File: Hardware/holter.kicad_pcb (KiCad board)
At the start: 6 copper layers, 33.5 x 48 mm, 261 parts, among them CN1 2TAP, CN2 2TAP, CN3 3TAP, IC1 256kx8, M1 USB_Power_Module, M2 USB_Power_Module, P1 CONN_01X07, P2 PROG, P3 SCREW, P4 BAT-, Q1 PMF170XP, Q2 PMF170XP, Q3 NTR4101PT1G, Q4 PMF170XP, Q5 PMF170XP, U1 TXB0106, U10 TS5A3159, U11 TS5A3159, U12 ESD_PROTECTOR, U13 ESD_PROTECTOR, U14 ESD_PROTECTOR, U15 ESD_PROTECTOR, U16 ESD_PROTECTOR, U17 ESD_PROTECTOR, U18 ESD_PROTECTOR, U19 ESD_PROTECTOR, U2 TXB0106, U20 ESD_PROTECTOR, U21 ESD_PROTECTOR, U22 ESD_PROTECTOR, U23 ESD_PROTECTOR, U24 TLV61220, U25 TLV61220, U26 TLV61220, U27 LM3671, U28 DS2710, U29 LIS2DH12, U3 TiWi-uB2, U4 STM32F4x1_64, U5 uSD, U6 ADS1298, U7 USBULC6-2M6, U8 USB2641, U9 OPA379, X1 32768, Y1 24 MHz, Y2 10 MHz

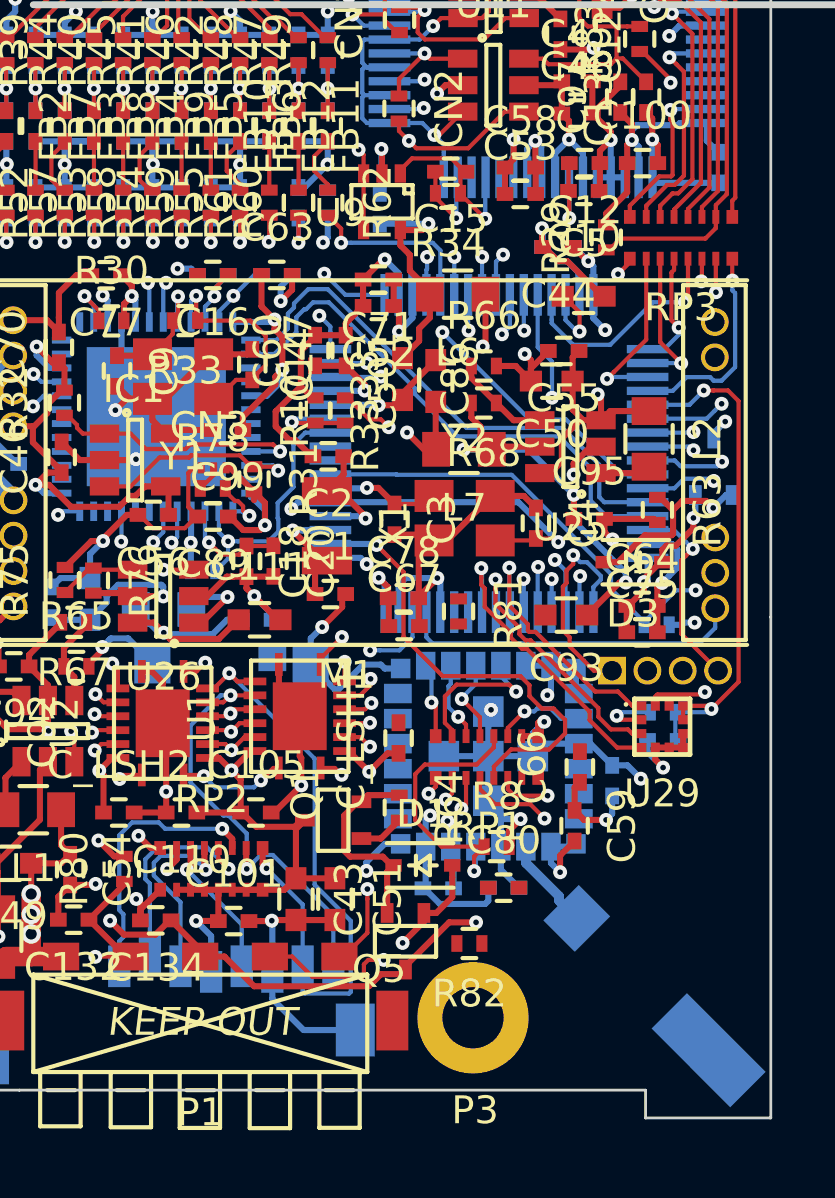
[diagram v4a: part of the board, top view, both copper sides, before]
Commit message: More PCB traces.
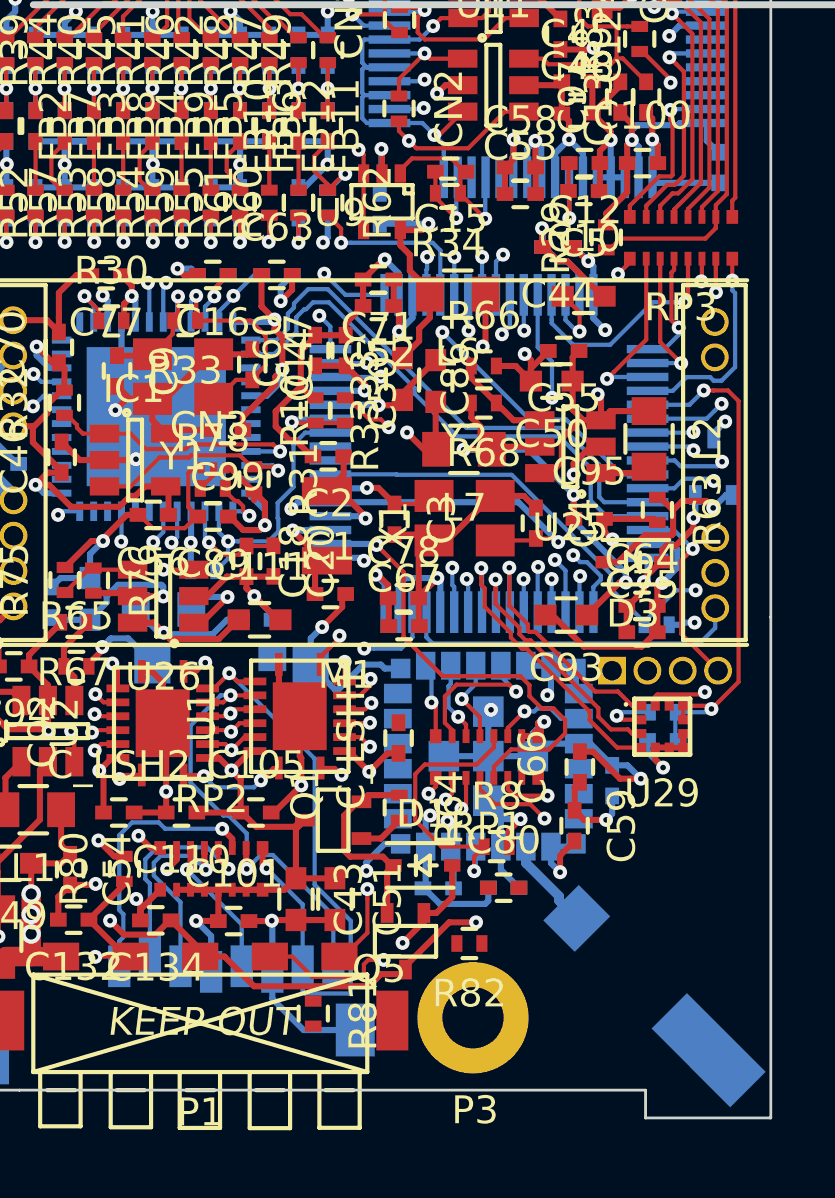
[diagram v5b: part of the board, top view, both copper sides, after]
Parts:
- moved R81 15.4 mm to (88.6, 79.2)
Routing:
- net GND: track 263.4 -> 271.5 mm
- net Net-(FB13-Pad1): track 2.16 -> 3.90 mm, vias 0 -> 1
- net G_PWM: track 0.00 -> 1.63 mm, vias 0 -> 1
- net R_PWM: track 0.00 -> 1.21 mm, vias 0 -> 1
- net SDIO_D1: track 18.8 -> 19.6 mm
- net SDIO_D2: track 13.4 -> 14.1 mm
- net SWCLK: track 8.13 -> 7.56 mm
- net SDIO_D0: track 18.7 -> 19.3 mm
- net RX: track 32.7 -> 32.2 mm

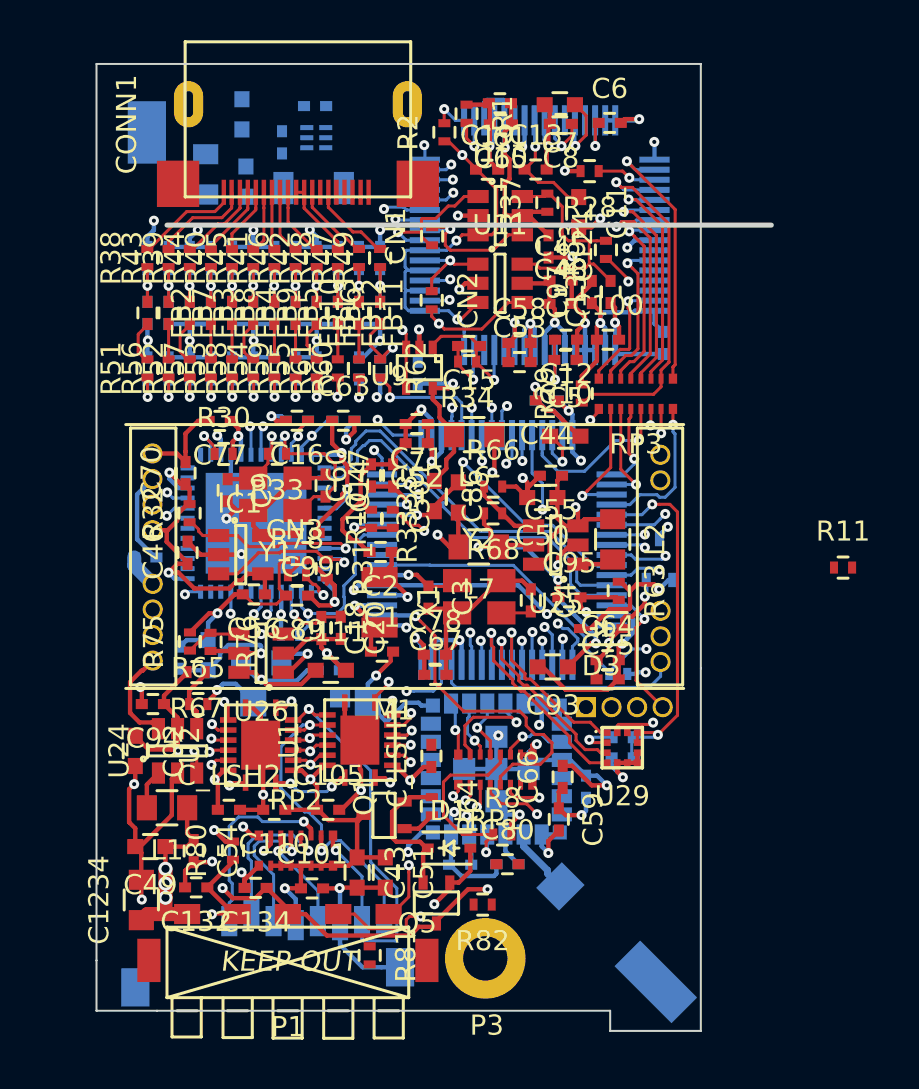
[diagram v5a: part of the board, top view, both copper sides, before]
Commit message: Everything is connected on the main board.
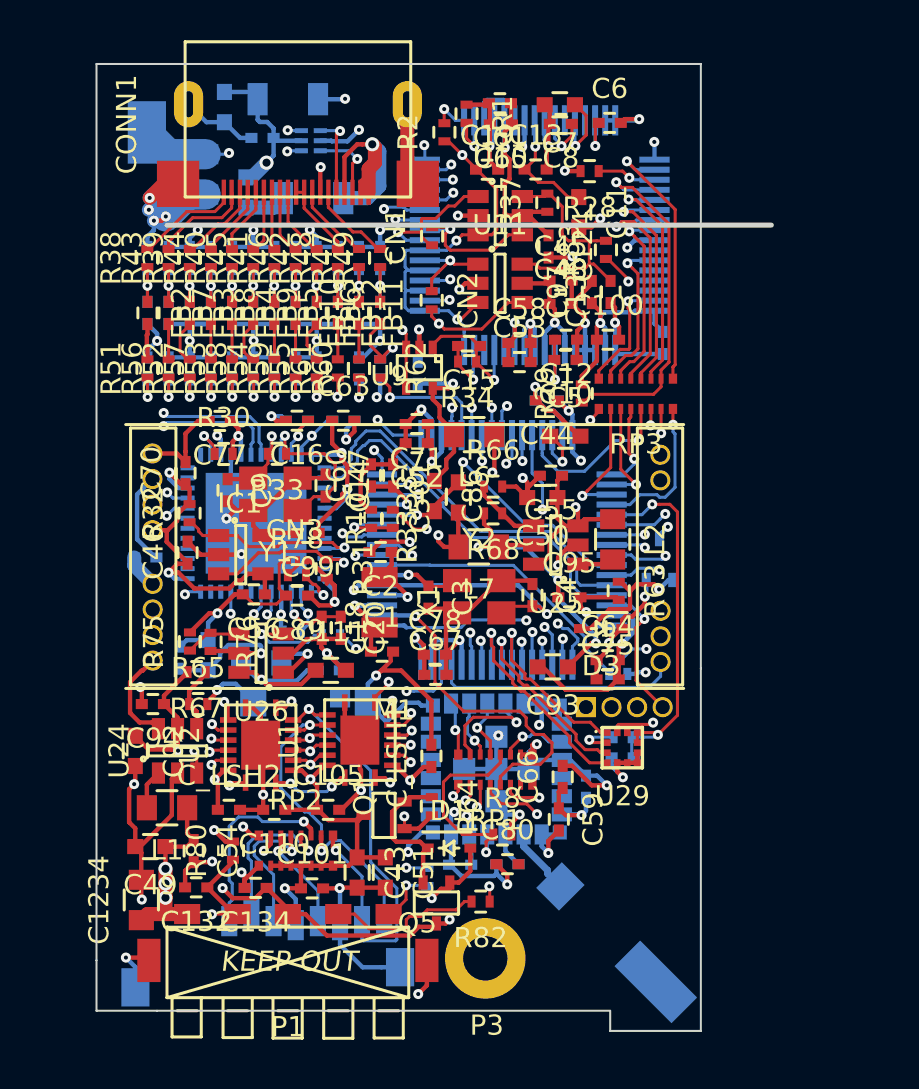
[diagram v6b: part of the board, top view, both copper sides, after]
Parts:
- C125: value 100nF -> 47uF; footprint Capacitors_SMD:C_0402 -> Capacitors_SMD:C_1206
- R11, R81: moved to B.Cu
- moved R11 25.6 mm to (86.6, 63.4), turned to 180 degrees
- moved R81 4.83 mm to (91.4, 75.4)
- moved C125 1.39 mm to (84.5, 36.8)
- moved C137 0.99 mm to (83.2, 38.7), turned to 180 degrees
- moved C115 0.94 mm to (81.3, 37.1)
- moved FB1 0.54 mm to (82.4, 41.4)
- moved F1 0.50 mm to (85.8, 41.7)
- moved U7 0.31 mm to (85.6, 38.8)
- moved C4 0.27 mm to (96.6, 61.4)
- moved R36 0.18 mm to (84.7, 63.2)
- moved R82 0.18 mm to (94.1, 76.6)
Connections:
- net DM renamed D-
- net DP renamed D+
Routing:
- net GND: track 271.5 -> 308.9 mm, vias 58 -> 67
- net R_PWM: track 1.21 -> 23.4 mm, vias 1 -> 2
- net +3V3: track 110.3 -> 131.1 mm
- net +5V: track 50.4 -> 68.2 mm, vias 2 -> 3
- net ~SD_EN: track 1.63 -> 18.7 mm, vias 0 -> 2
- net G_PWM: track 1.63 -> 18.3 mm, vias 1 -> 2
- net BAT+: track 60.2 -> 74.5 mm
- net VBAT: track 1.25 -> 14.6 mm
- net Net-(CONN1-Pad16): track 0.00 -> 12.8 mm, vias 0 -> 1
- net Net-(R11-Pad1): track 0.00 -> 10.2 mm, vias 0 -> 2
- net +2.8VD: track 44.5 -> 54.7 mm
- net D+: track 18.5 -> 28.5 mm, vias 1 -> 2
- net D-: track 18.4 -> 28.1 mm, vias 1 -> 2
- net Net-(M1-Pad3): track 24.5 -> 33.1 mm, vias 0 -> 1
- net VCPU: track 45.1 -> 53.2 mm
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
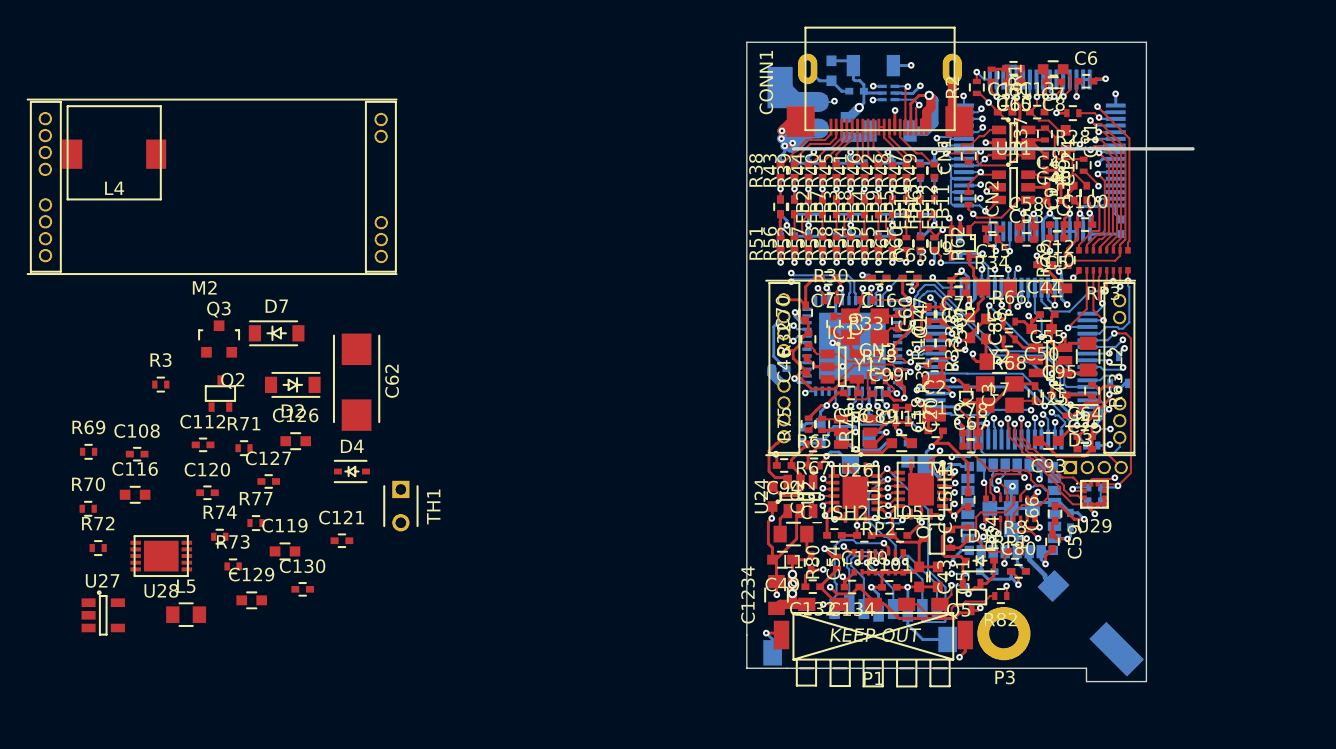
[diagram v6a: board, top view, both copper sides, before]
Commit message: New footprint for the inductor of the charger.
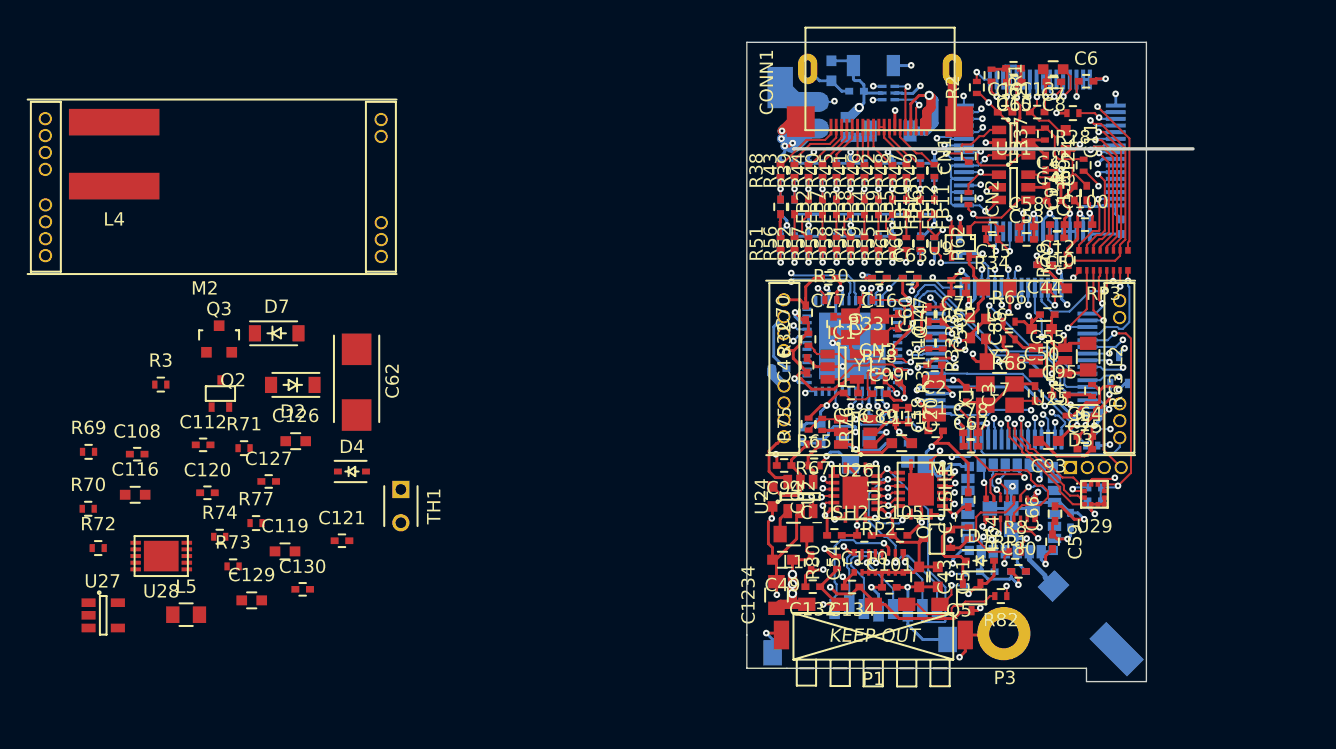
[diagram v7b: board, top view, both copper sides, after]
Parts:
- L4: value 15uH SLF7055T-150M2R1-3PF -> 15uH SRR6038; footprint Footprints:SLF7055 -> Footprints:SRR6038
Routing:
- net GND: track 308.9 -> 311.9 mm
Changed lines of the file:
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@@
   (general
     (links 682)
-    (no_connects 68)
-    (area 15.2726 20.8 109.150001 85.650001)
+    (no_connects 66)
+    (area 74.949999 34.949999 105.050001 83.050001)
     (thickness 1.6)
     (drawings 77)
-    (tracks 2962)
+    (tracks 2964)
     (zones 0)
     (modules 261)
@@
     )
   )
-  (module Footprints:SLF7055 (layer Front)
-    (at 27.5 43.4)
-    (fp_text reference L4 (at 0 2.6) (layer F.SilkS)
-      (effects (font (size 1 1) (thickness 0.15)))
-    )
-    (fp_text value "15uH SLF7055T-150M2R1-3PF" (at 0 -2.6) (layer F.Fab)
-      (effects (font (size 1 1) (thickness 0.15)))
-    )
-    (fp_line (start 3.5 -3.6) (end -3.5 -3.6) (layer F.SilkS) (width 0.15))
-    (fp_line (start 3.5 3.4) (end 3.5 -3.6) (layer F.SilkS) (width 0.15))
-    (fp_line (start -3.5 3.4) (end 3.5 3.4) (layer F.SilkS) (width 0.15))
-    (fp_line (start -3.5 -3.6) (end -3.5 3.4) (layer F.SilkS) (width 0.15))
-    (pad 1 smd rect (at -3.15 0) (size 1.5 2.2) (layers Front F.Paste F.Mask)
-      (net 70 "Net-(D7-Pad1)"))
-    (pad 2 smd rect (at 3.15 0) (size 1.5 2.2) (layers Front F.Paste F.Mask)
-      (net 167 "Net-(C126-Pad1)"))
-  )
   (module Capacitors_SMD:C_0805 (layer Front)
     (at 32.9 77.975)
@@
     )
   )
+  (module Footprints:SRR6038 (layer Front)
+    (at 27.5 43.4)
+    (fp_text reference L4 (at 0 4.9) (layer F.SilkS)
+      (effects (font (size 1 1) (thickness 0.15)))
+    )
+    (fp_text value "15uH SRR6038" (at 0 -4.9) (layer F.Fab)
+      (effects (font (size 1 1) (thickness 0.15)))
+    )
+    (pad 1 smd rect (at 0 -2.4) (size 6.8 2) (layers Front F.Paste F.Mask)
+      (net 70 "Net-(D7-Pad1)"))
+    (pad 2 smd rect (at 0 2.4) (size 6.8 2) (layers Front F.Paste F.Mask)
+      (net 167 "Net-(C126-Pad1)"))
+  )
   (gr_line (start 92 36.5) (end 105 36.5) (layer Dwgs.User) (width 0.1))
   (gr_line (start 92 35) (end 92 36.5) (layer Dwgs.User) (width 0.1))
@@
   (segment (start 89.175 61.875) (end 88.205 61.875) (width 0.22) (layer Back) (net 1))
   (segment (start 88.205 61.875) (end 88.19 61.89) (width 0.22) (layer Back) (net 1))
+  (segment (start 91.4 79.5) (end 94.2 79.5) (width 0.22) (layer Front) (net 2))
+  (segment (start 94.2 79.5) (end 94.3 79.4) (width 0.22) (layer Front) (net 2))
   (segment (start 95.1 60.65) (end 96.47 60.65) (width 0.22) (layer Front) (net 2))
   (segment (start 96.47 60.65) (end 96.64 60.82) (width 0.22) (layer Front) (net 2))

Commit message: Main board differential pairs + screw.
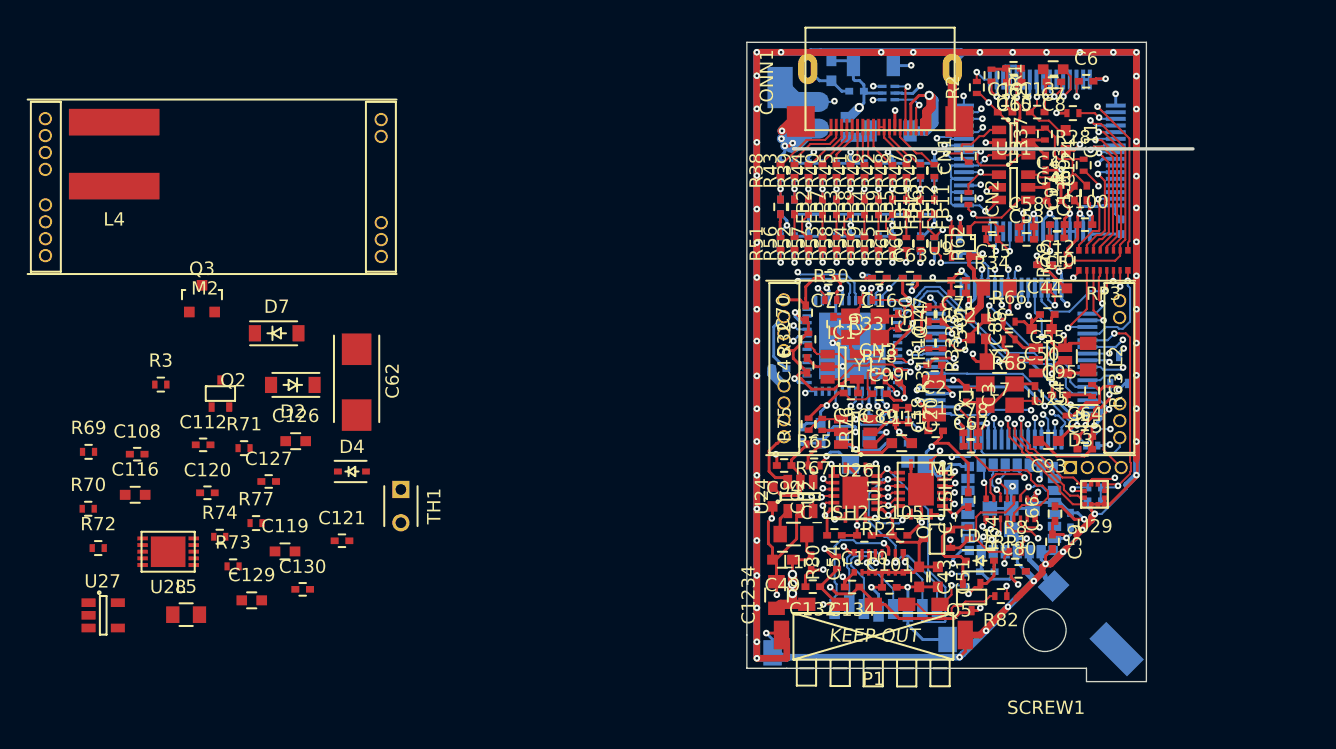
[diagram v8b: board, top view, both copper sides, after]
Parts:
- removed P3: SCREW, Footprints:M2_SCREW
- added SCREW1: SCREW, Footprints:M3_SCREW, F.Cu at (97.4, 79.2)
- moved Q3 3.29 mm to (34.1, 54.2)
- moved U28 0.61 mm to (31.6, 73.2)
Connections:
- net MCU_USB_DM renamed MCU_USB_D-
- net MCU_USB_DP renamed MCU_USB_D+
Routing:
- net GND: track 311.9 -> 598.1 mm, vias 67 -> 114
- net +3V3: track 131.1 -> 162.2 mm
- net +1V8: track 87.3 -> 105.9 mm
- net BAT+: track 74.5 -> 87.8 mm
- net +2.8VA: track 48.5 -> 51.7 mm
- net MCU_USB_D-: track 19.3 -> 18.6 mm
- net +5V: track 68.2 -> 68.8 mm
- net SDIO_CMD: track 11.1 -> 11.6 mm
- added copper zone on Power, net GND
